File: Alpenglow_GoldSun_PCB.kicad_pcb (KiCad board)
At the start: 2 copper layers, 52.4 x 52.4 mm, 10 parts, among them SW1 SW_SPDT

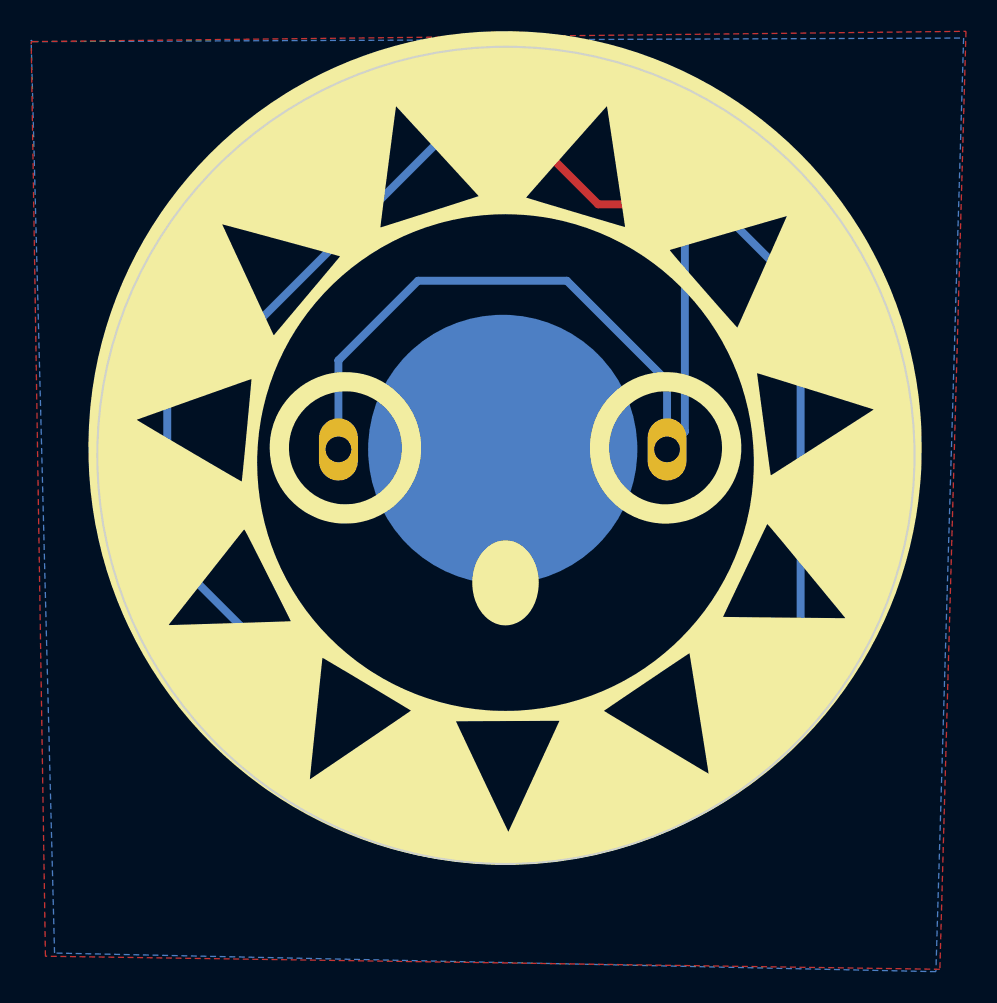
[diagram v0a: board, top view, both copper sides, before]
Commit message: Changed Sun to be exposed copper.  Added via so trace isn't going over exposed copper.
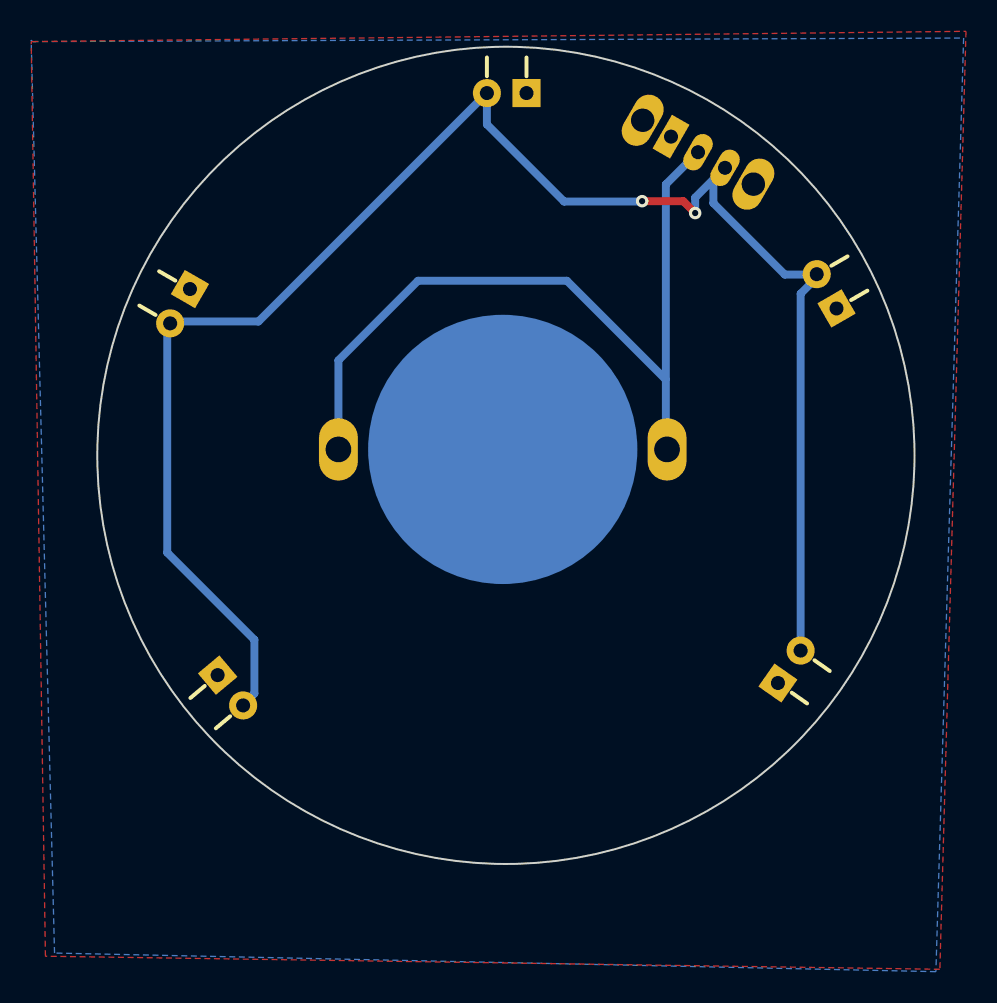
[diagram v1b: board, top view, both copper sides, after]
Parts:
- removed the G*** at (152.6, 90.8)
- added G***: LOGO, Alpenglow_Sun_PCB:NEW Sun 60, F.Cu at (152.5, 91.0)
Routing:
- net VCC: track 55.9 -> 51.4 mm
- net Net-(D1-Pad2): track 109.2 -> 111.4 mm, vias 0 -> 2
